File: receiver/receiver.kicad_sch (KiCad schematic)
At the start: 71 parts, among them J1 USB_B_Mini, J2 Conn_01x04_Pin, J3 Conn_01x04_Pin, SW1 SW_Push, SW2 SW_SPDT, U1 AMS1117-3.3, U2 STM32F303K8Tx, U3 MAX2622, U4 HMC356, U5 LT5517, U6 MABAES0054, U7 FT232RL, Y1 16MHz

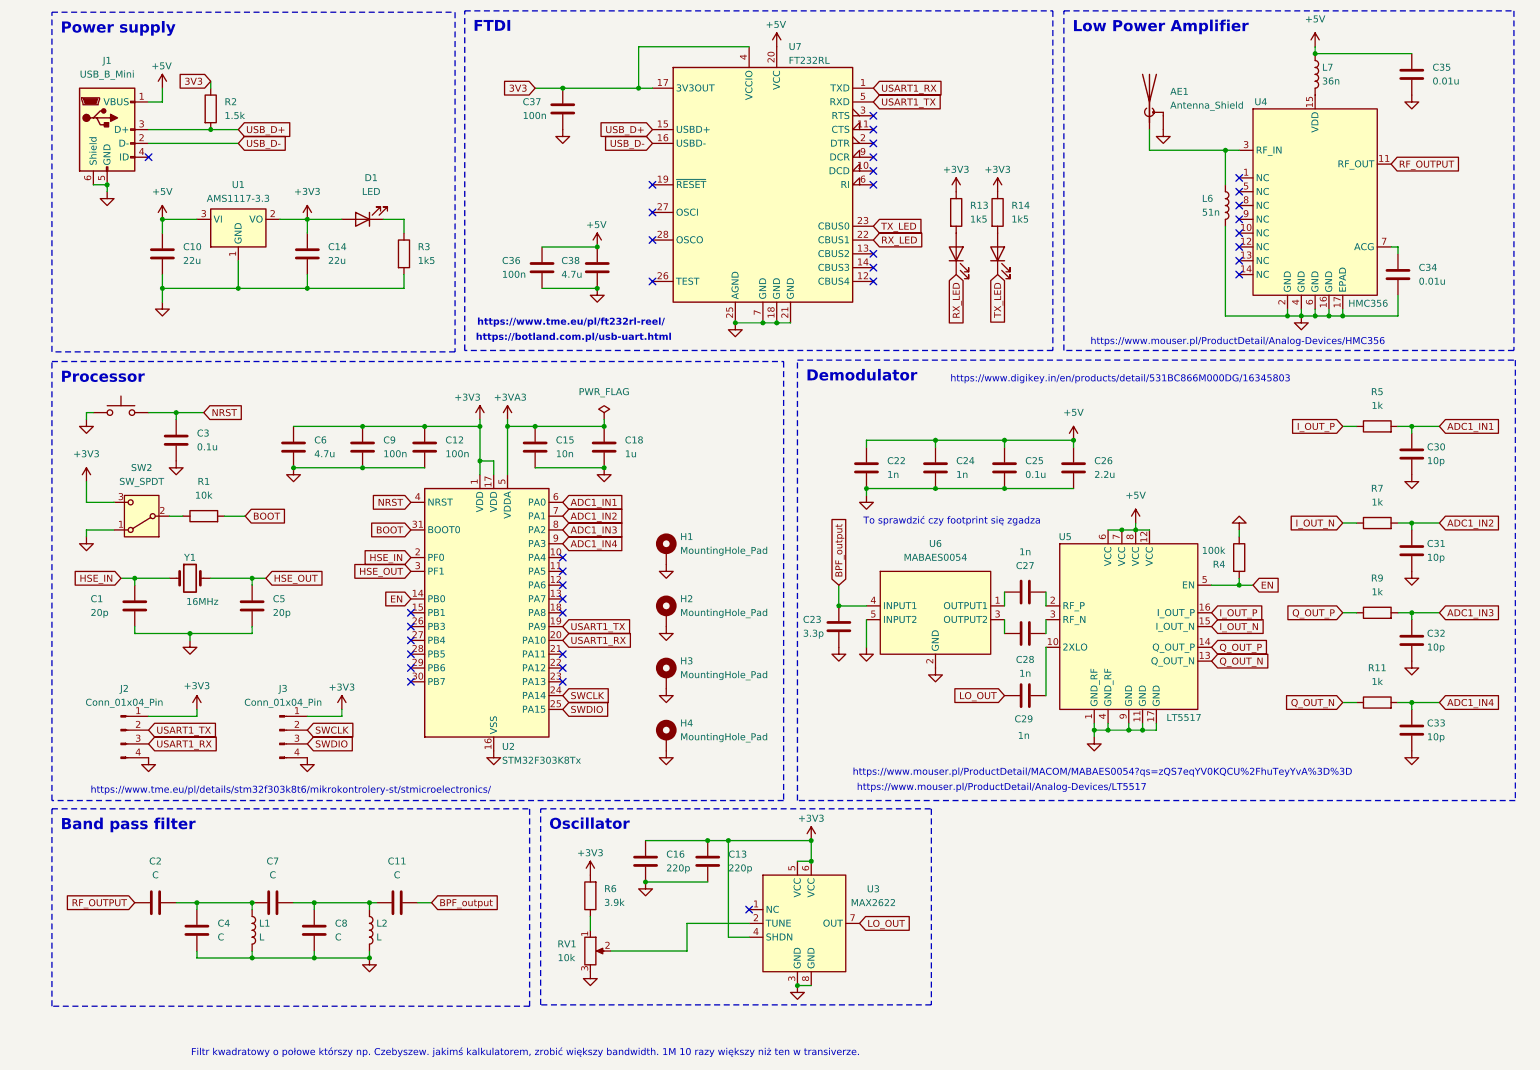
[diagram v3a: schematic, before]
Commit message: Correction to PCBs
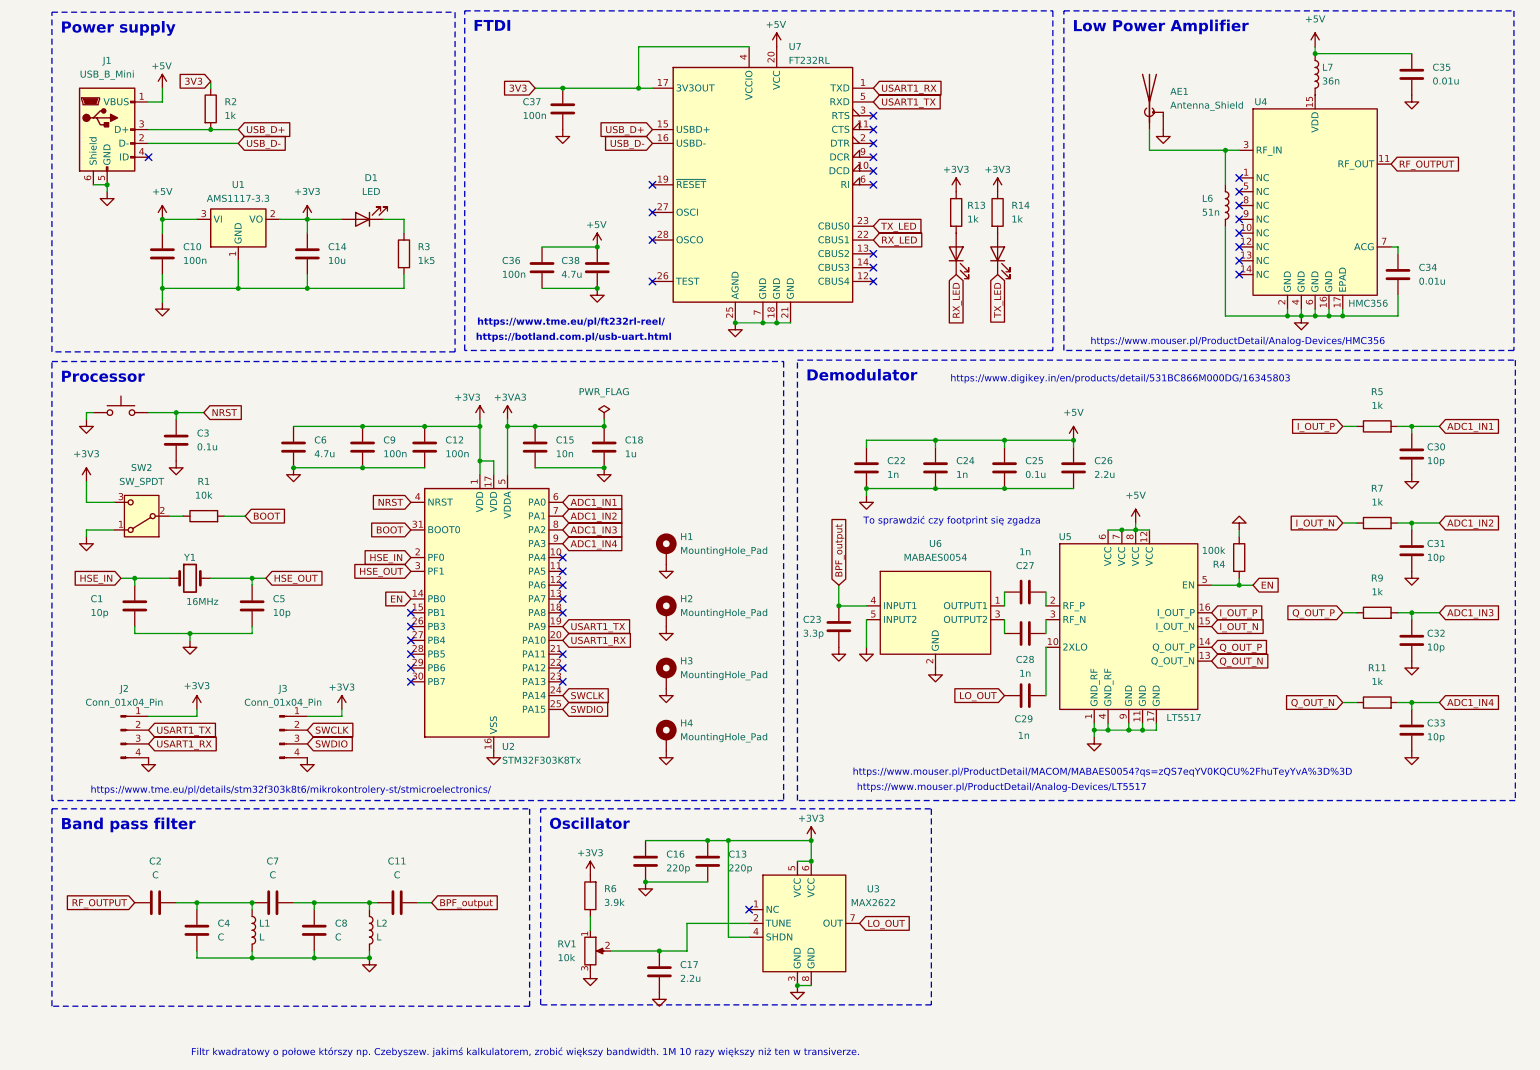
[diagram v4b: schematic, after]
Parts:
- added C17: 2.2u, Capacitor_SMD:C_0603_1608Metric_Pad1.08x0.95mm_HandSolder, symbol Device:C
- C1, C5: value 20p -> 10p
- C10: value 22u -> 100n
- C14: value 22u -> 10u
- R13, R14: value 1k5 -> 1k
- R2: value 1.5k -> 1k
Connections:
- net GND: now also C17.2
- net at RV1.2, U3.2 (TUNE): now also C17.1
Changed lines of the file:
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@@
 	)
 	(junction
+		(at 125.73 186.69)
+		(diameter 0)
+		(color 0 0 0 0)
+	)
+	(junction
 		(at 246.38 69.85)
 		(diameter 0)
@@
 	(wire
 		(pts
-			(xy 130.81 186.69) (xy 116.84 186.69)
+			(xy 130.81 186.69) (xy 125.73 186.69)
 		)
 		(stroke
@@
 	(wire
 		(pts
+			(xy 125.73 186.69) (xy 116.84 186.69)
+		)
+		(stroke
+			(width 0)
+			(type default)
+		)
+	)
+	(wire
+		(pts
 			(xy 34.29 52.07) (xy 34.29 54.61)
 		)
@@
 			)
 		)
-		(property "Value" "22u"
+		(property "Value" "100n"
 			(at 38.1 59.6899 0)
 			(effects
@@
 		(on_board yes)
 		(dnp no)
-		(fields_autoplaced yes)
 		(property "Reference" "R13"
-			(at 182.88 49.5299 0)
+			(at 182.372 49.53 0)
 			(effects
 				(font
@@
 			)
 		)
-		(property "Value" "1k5"
-			(at 182.88 52.0699 0)
+		(property "Value" "1k"
+			(at 182.372 52.07 0)
 			(effects
 				(font
@@
 			)
 		)
-		(property "Value" "20p"
+		(property "Value" "10p"
 			(at 54.61 124.4599 0)
 			(effects
@@
 			)
 		)
-		(property "Value" "22u"
+		(property "Value" "10u"
 			(at 64.77 59.6899 0)
 			(effects
@@
 			)
 		)
-		(property "Value" "20p"
+		(property "Value" "10p"
 			(at 21.082 124.46 0)
 			(effects
@@
 			)
 		)
-		(property "Value" "1k5"
+		(property "Value" "1k"
 			(at 190.5 52.0699 0)
 			(effects
@@
 	)
 	(symbol
+		(lib_id "Device:C")
+		(at 125.73 190.5 0)
+		(unit 1)
+		(exclude_from_sim no)
+		(in_bom yes)
+		(on_board yes)
+		(dnp no)
+		(fields_autoplaced yes)
+		(property "Reference" "C17"
+			(at 129.54 189.2299 0)
+			(effects
+				(font
+					(size 1.27 1.27)
+				)
+				(justify left)
+			)
+		)
+		(property "Value" "2.2u"
+			(at 129.54 191.7699 0)
+			(effects
+				(font
+					(size 1.27 1.27)
+				)
+				(justify left)
+			)
+		)
+		(property "Footprint" "Capacitor_SMD:C_0603_1608Metric_Pad1.08x0.95mm_HandSolder"
+			(at 126.6952 194.31 0)
+			(effects
+				(font
+					(size 1.27 1.27)
+				)
+				(hide yes)
+			)
+		)
+		(property "Datasheet" "~"
+			(at 125.73 190.5 0)
+			(effects
+				(font
+					(size 1.27 1.27)
+				)
+				(hide yes)
+			)
+		)
+		(property "Description" "Unpolarized capacitor"
+			(at 125.73 190.5 0)
+			(effects
+				(font
+					(size 1.27 1.27)
+				)
+				(hide yes)
+			)
+		)
+		(pin "1"
+		)
+		(pin "2"
+		)
+		(instances
+			(project "receiver"
+				(path "/9c85b918-2477-4635-b284-aa7b3f9ff354"
+					(reference "C17")
+					(unit 1)
+				)
+			)
+		)
+	)
+	(symbol
 		(lib_id "Device:R")
 		(at 257.81 124.46 90)
@@
 			)
 		)
-		(property "Value" "1.5k"
+		(property "Value" "1k"
 			(at 45.72 33.0199 0)
 			(effects
@@
 					(unit 1)
 				)
+			)
+		)
+	)
+	(symbol
+		(lib_id "power:GND")
+		(at 125.73 194.31 0)
+		(unit 1)
+		(exclude_from_sim no)
+		(in_bom yes)
+		(on_board yes)
+		(dnp no)
+		(fields_autoplaced yes)
+		(property "Reference" "#PWR053"
+			(at 125.73 200.66 0)
+			(effects
+				(font
+					(size 1.27 1.27)
+				)
+				(hide yes)
+			)
+		)
+		(property "Value" "GND"
+			(at 125.73 199.39 0)
+			(effects
+				(font
+					(size 1.27 1.27)
+				)
+				(hide yes)
+			)
+		)
+		(property "Footprint" ""
+			(at 125.73 194.31 0)
+			(effects
+				(font
+					(size 1.27 1.27)
+				)
+				(hide yes)
+			)
+		)
+		(property "Datasheet" ""
+			(at 125.73 194.31 0)
+			(effects
+				(font
+					(size 1.27 1.27)
+				)
+				(hide yes)
+			)
+		)
+		(property "Description" "Power symbol creates a global label with name \"GND\" , ground"
+			(at 125.73 194.31 0)
+			(effects
+				(font
+					(size 1.27 1.27)
+				)
+				(hide yes)
+			)
+		)
+		(pin "1"
+		)
+		(instances
+			(project "receiver"
+				(path "/9c85b918-2477-4635-b284-aa7b3f9ff354"
+					(reference "#PWR053")
+					(unit 1)
+				)
